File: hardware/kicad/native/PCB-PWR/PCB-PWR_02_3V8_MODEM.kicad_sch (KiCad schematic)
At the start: 17 parts, among them U3 LMR604403SRAKR 3V8

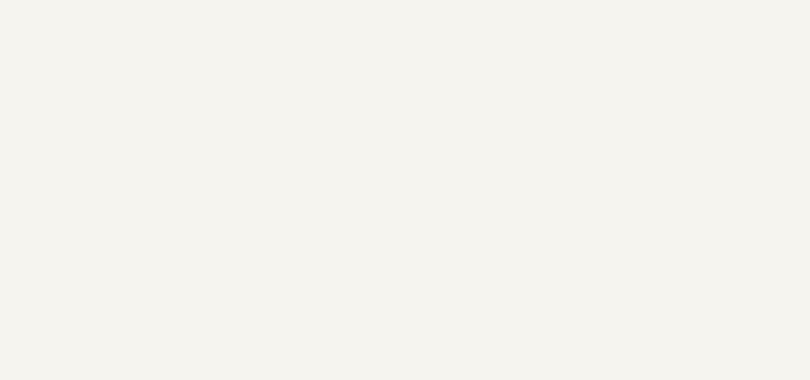
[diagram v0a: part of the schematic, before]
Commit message: pcb-pwr: add local buck input capacitors
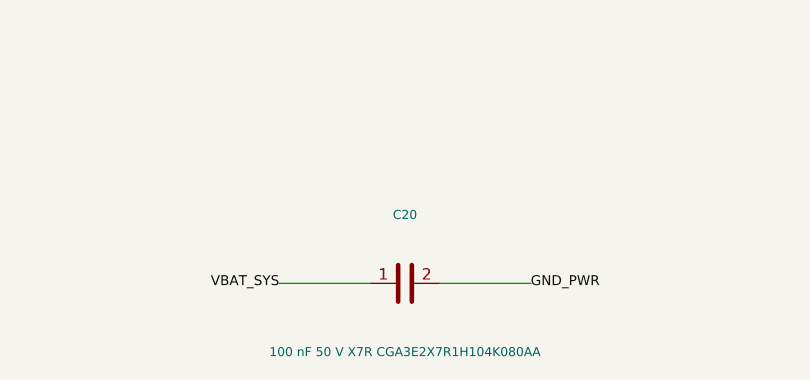
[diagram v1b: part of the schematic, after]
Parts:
- added C20: 100 nF 50 V X7R CGA3E2X7R1H104K080AA, Capacitor_SMD:C_0603_1608Metric, symbol Device:C
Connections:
- net GND_PWR: now also C20.2
- net VBAT_SYS: now also C20.1
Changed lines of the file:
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@@
   (title_block
     (title "Dioneya EVT-PRE-20 PCB-PWR Rev.A - 3V8 modem rail")
-    (date "2026-09-16")
+    (date "2026-09-17")
     (rev "A")
     (company "Dioneya / ZS-BPLA")
@@
     (stroke (width 0.0))
   )
+  (wire (pts (xy 153.67 238.76) (xy 143.51 238.76))
+    (stroke (width 0.0))
+  )
+  (wire (pts (xy 161.29 238.76) (xy 171.45 238.76))
+    (stroke (width 0.0))
+  )
   (wire (pts (xy 250.19 99.06) (xy 240.03 99.06))
     (stroke (width 0.0))
@@
     (effects (font (size 1.1 1.1)))
   )
+  (label "VBAT_SYS" (at 143.51 238.76 180)
+    (effects (font (size 1.1 1.1)))
+  )
+  (label "GND_PWR" (at 171.45 238.76 0)
+    (effects (font (size 1.1 1.1)))
+  )
   (label "3V8_MODEM" (at 240.03 99.06 180)
     (effects (font (size 1.1 1.1)))
@@
         )
       )
+    )
+  )
+  (symbol (lib_id "Device:C") (at 157.48 238.76 90) (unit 1)
+    (in_bom yes) (on_board yes) (dnp no)
+    (property "Reference" "C20" (id 0) (at 157.48 231.14 270)
+      (effects (font (size 1.0 1.0)))
+    )
+    (property "Value" "100 nF 50 V X7R CGA3E2X7R1H104K080AA" (id 1) (at 157.48 246.38 270)
+      (effects (font (size 1.0 1.0)))
+    )
+    (property "Footprint" "Capacitor_SMD:C_0603_1608Metric" (id 2) (at 157.48 247.76 0)
+      (effects (font (size 1 1)) hide)
+    )
+    (property "Datasheet" "TDK exact product data for CGA3E2X7R1H104K080AA" (id 3) (at 157.48 249.76 0)
+      (effects (font (size 1 1)) hide)
+    )
+    (pin "1")
+    (pin "2")
+    (instances
+      (project "PCB-PWR"
+        (path "/630df535-af27-5a6d-b3fe-890f0243b40c/079baa7d-cb9e-5f99-8fa8-3059812ae49a"
+          (reference "C20") (unit 1)
+        )
+      )

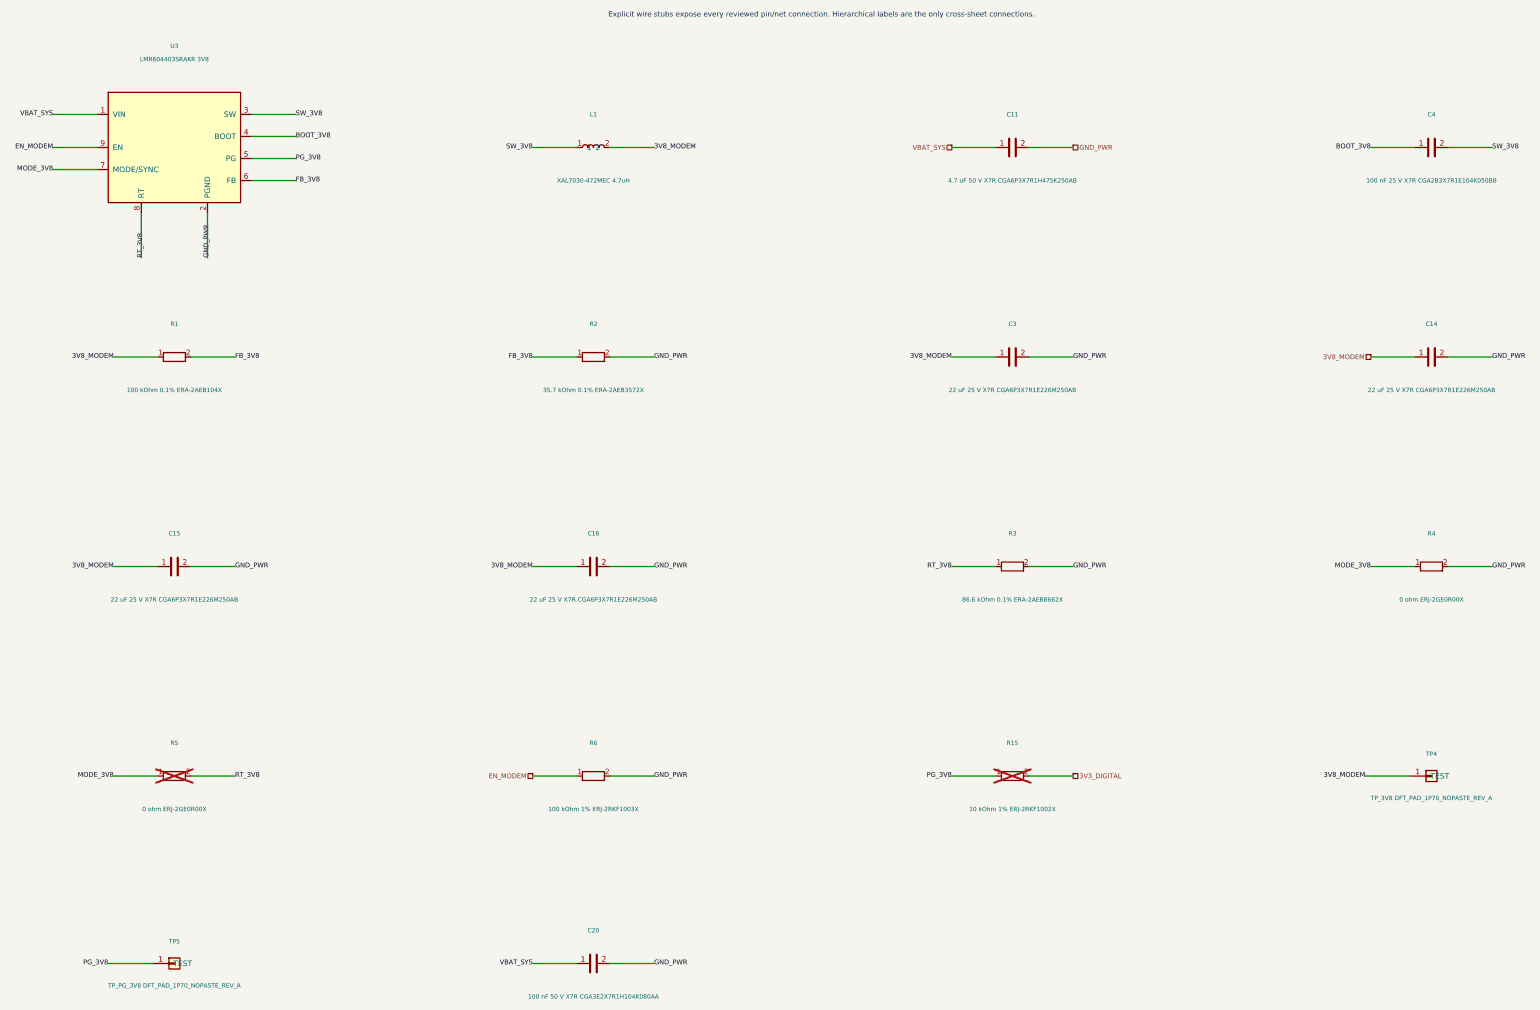
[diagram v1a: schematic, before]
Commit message: pcb-pwr: keep labels clear of connection wires
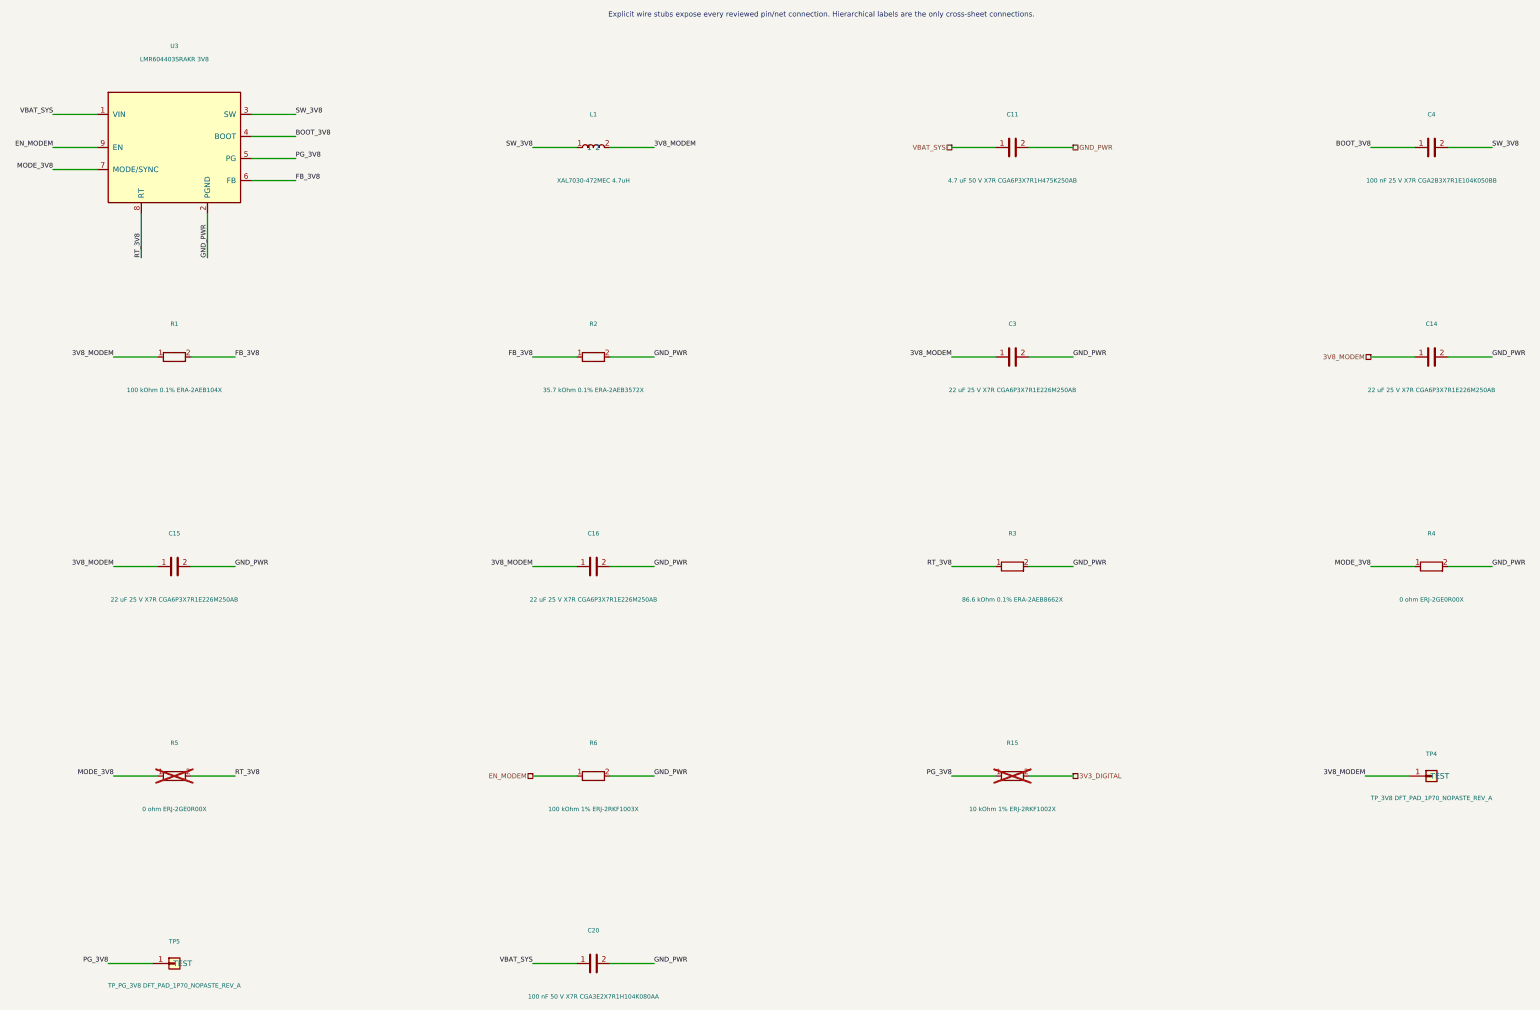
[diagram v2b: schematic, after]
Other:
- title: Dioneya EVT-PRE-20 PCB-PWR Rev.A - 3V8 modem rail -> 3V8 modem rail
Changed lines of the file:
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@@
   (paper "A3")
   (title_block
-    (title "Dioneya EVT-PRE-20 PCB-PWR Rev.A - 3V8 modem rail")
+    (title "3V8 modem rail")
     (date "2026-09-17")
     (rev "A")
@@
   )
   (label "GND_PWR" (at 364.49 99.06 0)
-    (effects (font (size 1.1 1.1)))
+    (effects (font (size 1.1 1.1)) (justify bottom))
   )
   (label "3V8_MODEM" (at 46.99 147.32 180)
-    (effects (font (size 1.1 1.1)))
+    (effects (font (size 1.1 1.1)) (justify bottom))
   )
   (label "GND_PWR" (at 74.93 147.32 0)
-    (effects (font (size 1.1 1.1)))
+    (effects (font (size 1.1 1.1)) (justify bottom))
   )
   (label "3V8_MODEM" (at 143.51 147.32 180)
-    (effects (font (size 1.1 1.1)))
+    (effects (font (size 1.1 1.1)) (justify bottom))
   )
   (label "GND_PWR" (at 171.45 147.32 0)
-    (effects (font (size 1.1 1.1)))
+    (effects (font (size 1.1 1.1)) (justify bottom))
   )
   (label "VBAT_SYS" (at 143.51 238.76 180)
-    (effects (font (size 1.1 1.1)))
+    (effects (font (size 1.1 1.1)) (justify bottom))
   )
   (label "GND_PWR" (at 171.45 238.76 0)
-    (effects (font (size 1.1 1.1)))
+    (effects (font (size 1.1 1.1)) (justify bottom))
   )
   (label "3V8_MODEM" (at 240.03 99.06 180)
-    (effects (font (size 1.1 1.1)))
+    (effects (font (size 1.1 1.1)) (justify bottom))
   )
   (label "GND_PWR" (at 267.97 99.06 0)
-    (effects (font (size 1.1 1.1)))
+    (effects (font (size 1.1 1.1)) (justify bottom))
   )
   (label "BOOT_3V8" (at 336.55 50.8 180)
-    (effects (font (size 1.1 1.1)))
+    (effects (font (size 1.1 1.1)) (justify bottom))
   )
   (label "SW_3V8" (at 364.49 50.8 0)
-    (effects (font (size 1.1 1.1)))
+    (effects (font (size 1.1 1.1)) (justify bottom))
   )
   (label "SW_3V8" (at 143.51 50.8 180)
-    (effects (font (size 1.1 1.1)))
+    (effects (font (size 1.1 1.1)) (justify bottom))
   )
   (label "3V8_MODEM" (at 171.45 50.8 0)
-    (effects (font (size 1.1 1.1)))
+    (effects (font (size 1.1 1.1)) (justify bottom))
   )
   (label "3V8_MODEM" (at 46.99 99.06 180)
-    (effects (font (size 1.1 1.1)))
+    (effects (font (size 1.1 1.1)) (justify bottom))
   )
   (label "FB_3V8" (at 74.93 99.06 0)
-    (effects (font (size 1.1 1.1)))
+    (effects (font (size 1.1 1.1)) (justify bottom))
   )
   (label "PG_3V8" (at 240.03 195.58 180)
-    (effects (font (size 1.1 1.1)))
+    (effects (font (size 1.1 1.1)) (justify bottom))
   )
   (label "FB_3V8" (at 143.51 99.06 180)
-    (effects (font (size 1.1 1.1)))
+    (effects (font (size 1.1 1.1)) (justify bottom))
   )
   (label "GND_PWR" (at 171.45 99.06 0)
-    (effects (font (size 1.1 1.1)))
+    (effects (font (size 1.1 1.1)) (justify bottom))
   )
   (label "RT_3V8" (at 240.03 147.32 180)
-    (effects (font (size 1.1 1.1)))
+    (effects (font (size 1.1 1.1)) (justify bottom))
   )
   (label "GND_PWR" (at 267.97 147.32 0)
-    (effects (font (size 1.1 1.1)))
+    (effects (font (size 1.1 1.1)) (justify bottom))
   )
   (label "MODE_3V8" (at 336.55 147.32 180)
-    (effects (font (size 1.1 1.1)))
+    (effects (font (size 1.1 1.1)) (justify bottom))
   )
   (label "GND_PWR" (at 364.49 147.32 0)
-    (effects (font (size 1.1 1.1)))
+    (effects (font (size 1.1 1.1)) (justify bottom))
   )
   (label "MODE_3V8" (at 46.99 195.58 180)
-    (effects (font (size 1.1 1.1)))
+    (effects (font (size 1.1 1.1)) (justify bottom))
   )
   (label "RT_3V8" (at 74.93 195.58 0)
-    (effects (font (size 1.1 1.1)))
+    (effects (font (size 1.1 1.1)) (justify bottom))
   )
   (label "GND_PWR" (at 171.45 195.58 0)
-    (effects (font (size 1.1 1.1)))
+    (effects (font (size 1.1 1.1)) (justify bottom))
   )
   (label "3V8_MODEM" (at 335.28 195.58 180)
-    (effects (font (size 1.1 1.1)))
+    (effects (font (size 1.1 1.1)) (justify bottom))
   )
   (label "PG_3V8" (at 45.72 238.76 180)
-    (effects (font (size 1.1 1.1)))
+    (effects (font (size 1.1 1.1)) (justify bottom))
   )
   (label "VBAT_SYS" (at 33.02 43.18 180)
-    (effects (font (size 1.1 1.1)))
+    (effects (font (size 1.1 1.1)) (justify bottom))
   )
   (label "GND_PWR" (at 68.58 76.2 90)
-    (effects (font (size 1.1 1.1)))
+    (effects (font (size 1.1 1.1)) (justify bottom))
   )
   (label "SW_3V8" (at 88.9 43.18 0)
-    (effects (font (size 1.1 1.1)))
+    (effects (font (size 1.1 1.1)) (justify bottom))
   )
   (label "BOOT_3V8" (at 88.9 48.26 0)
-    (effects (font (size 1.1 1.1)))
+    (effects (font (size 1.1 1.1)) (justify bottom))
   )
   (label "PG_3V8" (at 88.9 53.34 0)
-    (effects (font (size 1.1 1.1)))
+    (effects (font (size 1.1 1.1)) (justify bottom))
   )
   (label "FB_3V8" (at 88.9 58.42 0)
-    (effects (font (size 1.1 1.1)))
+    (effects (font (size 1.1 1.1)) (justify bottom))
   )
   (label "MODE_3V8" (at 33.02 55.88 180)
-    (effects (font (size 1.1 1.1)))
+    (effects (font (size 1.1 1.1)) (justify bottom))
   )
   (label "RT_3V8" (at 53.34 76.2 90)
-    (effects (font (size 1.1 1.1)))
+    (effects (font (size 1.1 1.1)) (justify bottom))
   )
   (label "EN_MODEM" (at 33.02 50.8 180)
-    (effects (font (size 1.1 1.1)))
+    (effects (font (size 1.1 1.1)) (justify bottom))
   )
   (hierarchical_label "VBAT_SYS" (shape passive) (at 240.03 50.8 180)
-    (effects (font (size 1.1 1.1)))
+    (effects (font (size 1.1 1.1)) (justify bottom))
   )
   (hierarchical_label "GND_PWR" (shape passive) (at 267.97 50.8 0)
-    (effects (font (size 1.1 1.1)))
+    (effects (font (size 1.1 1.1)) (justify bottom))
   )
   (hierarchical_label "3V8_MODEM" (shape passive) (at 336.55 99.06 180)
-    (effects (font (size 1.1 1.1)))
+    (effects (font (size 1.1 1.1)) (justify bottom))
   )
   (hierarchical_label "3V3_DIGITAL" (shape passive) (at 267.97 195.58 0)
-    (effects (font (size 1.1 1.1)))
+    (effects (font (size 1.1 1.1)) (justify bottom))
   )
   (hierarchical_label "EN_MODEM" (shape passive) (at 143.51 195.58 180)
-    (effects (font (size 1.1 1.1)))
+    (effects (font (size 1.1 1.1)) (justify bottom))
   )
   (symbol (lib_id "Device:C") (at 254.0 50.8 90) (unit 1)
